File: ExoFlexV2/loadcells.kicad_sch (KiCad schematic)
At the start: 73 parts, among them U14 SN74LVC3G14DCUT_V2, U16 SN74LV4T08PWR_V2, U17 SN74HC7032D_V2, U24 MCP6001T-I_OT, U25 MCP6001T-I_OT, U26 MCP6001T-I_OT, U27 ADCMP602BRMZ, U28 ADCMP602BRMZ, U29 ADCMP602BRMZ

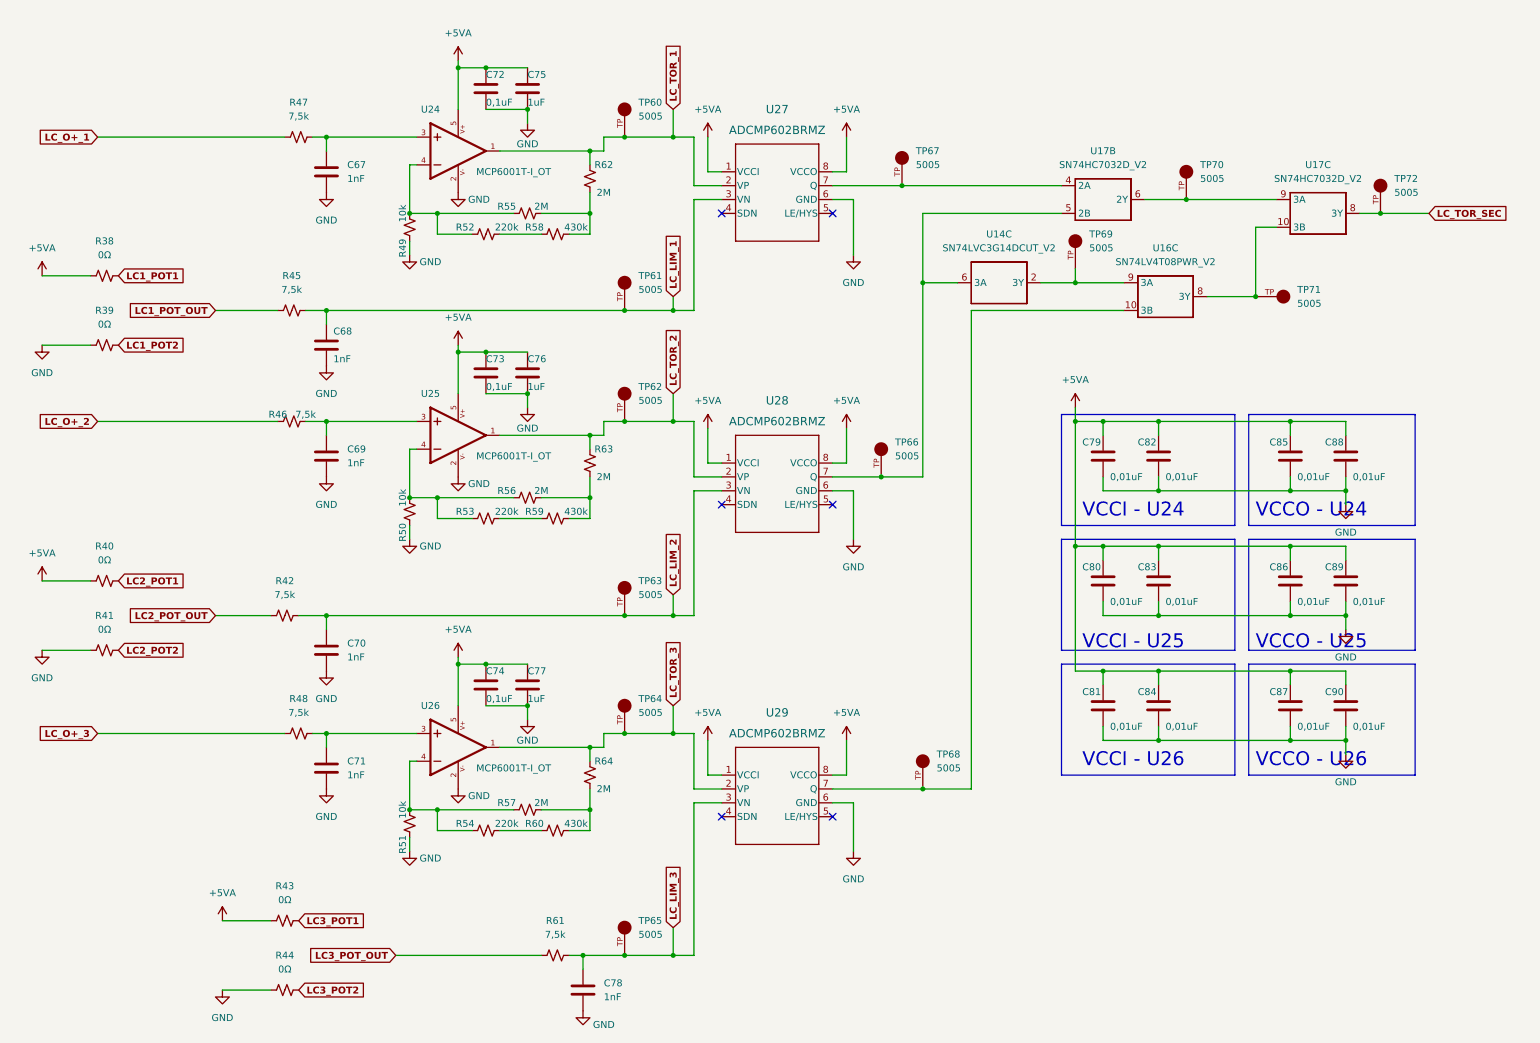
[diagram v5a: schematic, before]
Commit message: Mise à jour mi-stage
- Torque et Amplitude testé et vérifié
- Capteur de présence et de proximité testé
- Système de détection de coupure de fils
- Polyvalence pour plusieurs capteurs
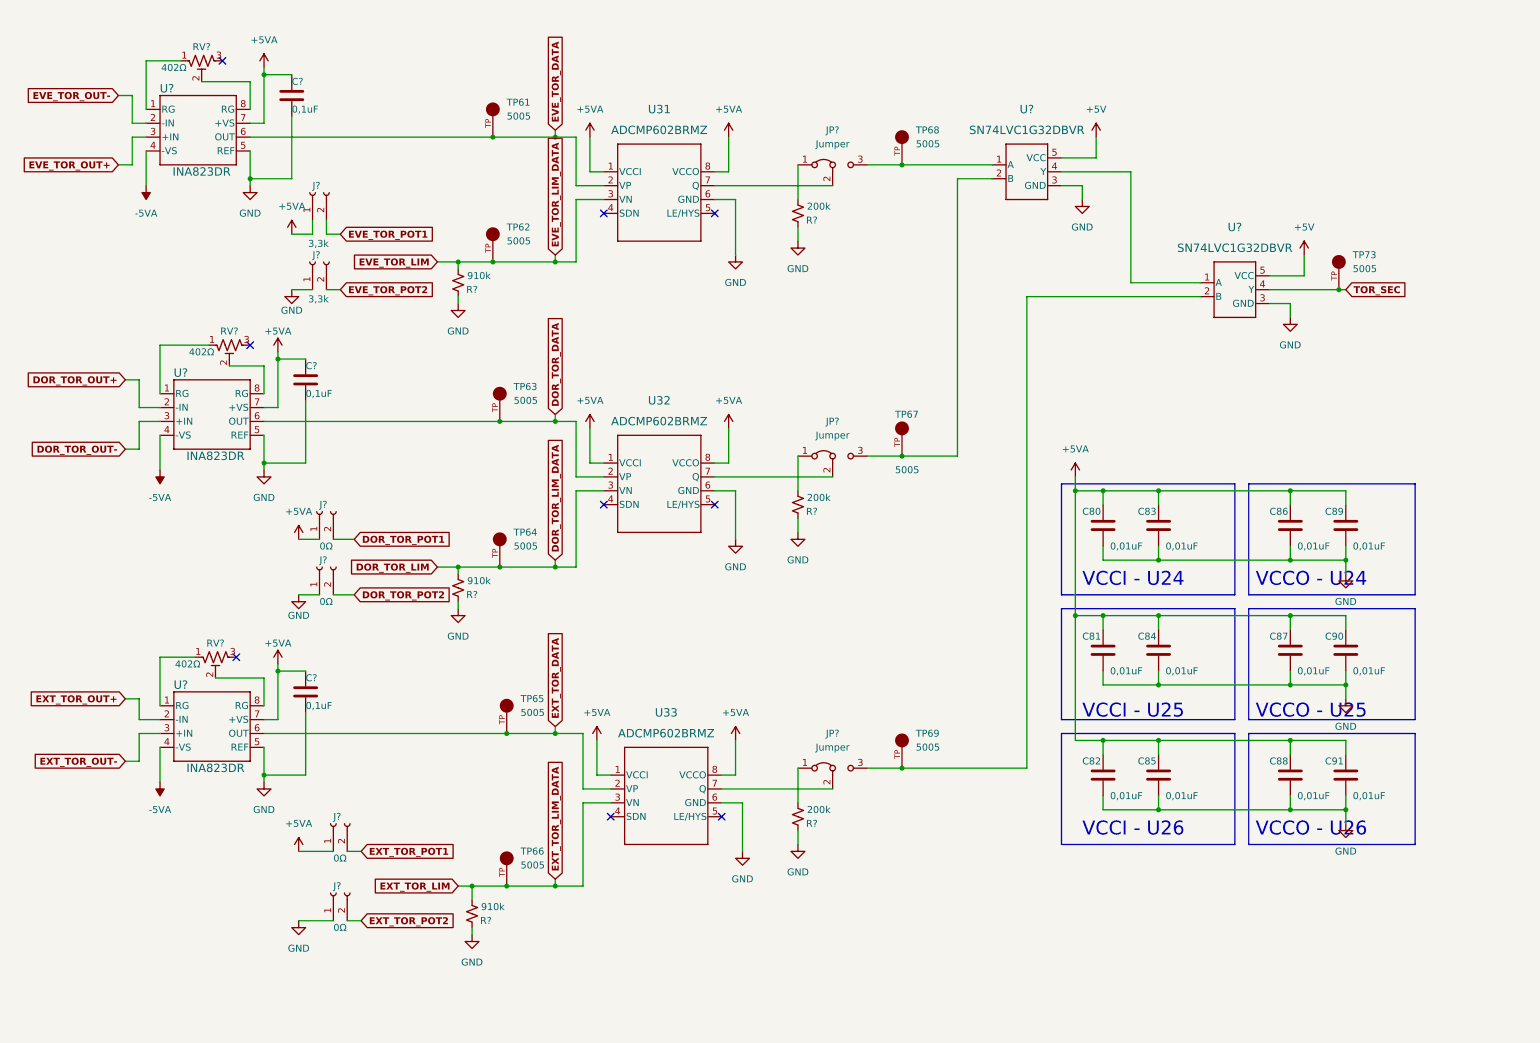
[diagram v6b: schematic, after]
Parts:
- removed C67, C68, C69, C70, C71, C78: 1nF, Capacitor_SMD:C_0603_1608Metric, symbol Device:C
- removed C72, C73, C74: 0,1uF, Capacitor_SMD:C_0603_1608Metric, symbol Device:C
- removed C75, C76, C77: 1uF, Capacitor_SMD:C_0603_1608Metric, symbol Device:C
- removed R38, R39, R40, R41, R43, R44: 0Ω, Resistor_SMD:R_0603_1608Metric, symbol Device:R_Small_US
- removed R42, R45, R46, R47, R48, R61: 7,5k, Resistor_SMD:R_0603_1608Metric, symbol Device:R_Small_US
- removed R49, R50, R51: 10k, Resistor_SMD:R_0603_1608Metric, symbol Device:R_Small_US
- removed R52, R53, R54: 220k, Resistor_SMD:R_0603_1608Metric, symbol Device:R_Small_US
- removed R55, R56, R57, R62, R63, R64: 2M, Resistor_SMD:R_0603_1608Metric, symbol Device:R_Small_US
- removed R58, R59, R60: 430k, Resistor_SMD:R_0603_1608Metric, symbol Device:R_Small_US
- removed TP69, TP70, TP71: 5005, FootPrint:KEYSTONE_5005, symbol SymLib:5005
- removed U14: SN74LVC3G14DCUT_V2, FootPrint:SN74LVC3G14DCUT, symbol SymLib:SN74LVC3G14DCUT_V2
- removed U16: SN74LV4T08PWR_V2, FootPrint:SN74LV4T08PWR, symbol SymLib:SN74LV4T08PWR_V2
- removed U17: SN74HC7032D_V2, FootPrint:SN74HC7032D, symbol SymLib:SN74HC7032D_V2
- removed U24, U25, U26: MCP6001T-I_OT, FootPrint:SOT95P270X145-5N, symbol SymLib:MCP6001T-I_OT
- added C? (x3): 0,1uF, Capacitor_SMD:C_0402_1005Metric, symbol Device:C
- added J? (x2): 3,3k, Connector_PinHeader_2.54mm:PinHeader_1x02_P2.54mm_Vertical, symbol Connector:Conn_01x02_Female
- added J? (x4): 0Ω, Connector_PinHeader_2.54mm:PinHeader_1x02_P2.54mm_Vertical, symbol Connector:Conn_01x02_Female
- added JP? (x3): Jumper, Connector_PinHeader_2.54mm:PinHeader_1x03_P2.54mm_Vertical, symbol Jumper:Jumper_3_Bridged12
- added R? (x3): 200k, Resistor_SMD:R_0603_1608Metric, symbol Device:R_Small_US
- added R? (x3): 910k, Resistor_SMD:R_0603_1608Metric, symbol Device:R_Small_US
- added RV? (x3): 402Ω, FootPrint:TRIM_3362P-1-102LF, symbol Device:R_Potentiometer_Trim_US
- added U? (x3): INA823DR, FootPrint:D0008A_SOIC_TEX, symbol SymLib:INA823DR
- added U? (x2): SN74LVC1G32DBVR, FootPrint:SOT95P270X145-5N, symbol SymLib:SN74LVC1G32DBVR
- renumbered C79 to C80, C80 to C81, C81 to C82, C82 to C83, C83 to C84, C84 to C85, C85 to C86, C86 to C87, C87 to C88, C88 to C89, C89 to C90, C90 to C91, TP60 to TP61, TP61 to TP62, TP62 to TP63, TP63 to TP64, TP64 to TP65, TP65 to TP66, TP66 to TP67, TP67 to TP68, TP68 to TP69, TP72 to TP73, U27 to U31, U28 to U32, U29 to U33
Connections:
- net +5VA: now also C?.1, C?.1, C?.1, J?.1 (Pin_1), J?.1 (Pin_1), J?.1 (Pin_1), U?.7 (+VS), U?.7 (+VS), U?.7 (+VS)
- net GND: now also C?.2, C?.2, C?.2, J?.1 (Pin_1), J?.1 (Pin_1), J?.1 (Pin_1), R?.2, R?.2, R?.2, R?.2, R?.2, R?.2, U?.3 (GND), U?.3 (GND), U?.5 (REF), U?.5 (REF), U?.5 (REF)
- net at TP67.TP: now also JP?.3 (B), U?.2 (B); no longer U32.7 (Q)
- net at U33.7 (Q): now also JP?.2 (C); no longer TP69.TP
- net at TP68.TP: now also JP?.3 (B), U?.1 (A); no longer U31.7 (Q)
- net LC_LIM_1 renamed EVE_TOR_LIM
- net EVE_TOR_LIM: now also R?.1
- net LC_LIM_2 renamed DOR_TOR_LIM
- net DOR_TOR_LIM: now also R?.1
- net LC_LIM_3 renamed EXT_TOR_LIM
- net EXT_TOR_LIM: now also R?.1
- net LC_TOR_1 renamed EVE_TOR_DATA
- net EVE_TOR_DATA: now also U?.6 (OUT)
- net LC_TOR_2 renamed DOR_TOR_DATA
- net DOR_TOR_DATA: now also U?.6 (OUT)
- net LC_TOR_3 renamed EXT_TOR_DATA
- net EXT_TOR_DATA: now also U?.6 (OUT)
- net LC_TOR_SEC renamed TOR_SEC
- net TOR_SEC: now also U?.4 (Y)
- new net: JP?.1 (A), R?.1 (x3)
- new net: RV?.1, U?.1 (RG) (x3)
- new net: RV?.2, U?.8 (RG) (x3)
- new net: JP?.3 (B), TP69.TP, U?.2 (B)
- new net: U?.1 (A), U?.4 (Y)
- new net: JP?.2 (C), U32.7 (Q)
- new net: JP?.2 (C), U31.7 (Q)
- new net +5V: U?.5 (VCC), U?.5 (VCC)
- new net -5VA: U?.4 (-VS), U?.4 (-VS), U?.4 (-VS)
- new net DOR_TOR_OUT+: U?.2 (-IN)
- new net DOR_TOR_OUT-: U?.3 (+IN)
- new net DOR_TOR_POT1: J?.2 (Pin_2)
- new net DOR_TOR_POT2: J?.2 (Pin_2)
- new net EVE_TOR_OUT+: U?.3 (+IN)
- new net EVE_TOR_OUT-: U?.2 (-IN)
- new net EVE_TOR_POT1: J?.2 (Pin_2)
- new net EVE_TOR_POT2: J?.2 (Pin_2)
- new net EXT_TOR_OUT+: U?.2 (-IN)
- new net EXT_TOR_OUT-: U?.3 (+IN)
- new net EXT_TOR_POT1: J?.2 (Pin_2)
- new net EXT_TOR_POT2: J?.2 (Pin_2)
- no-connect marks 6 -> 9
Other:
- moved on the sheet: C80, C81, C82, C83, C84, C85, C86, C87, C88, C89, C90, C91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

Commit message: Mise à jour signaux STM
- Condo de découplage
- Signaux supplémentaire pour le STM
- Page GND sera pour Multiplexeur
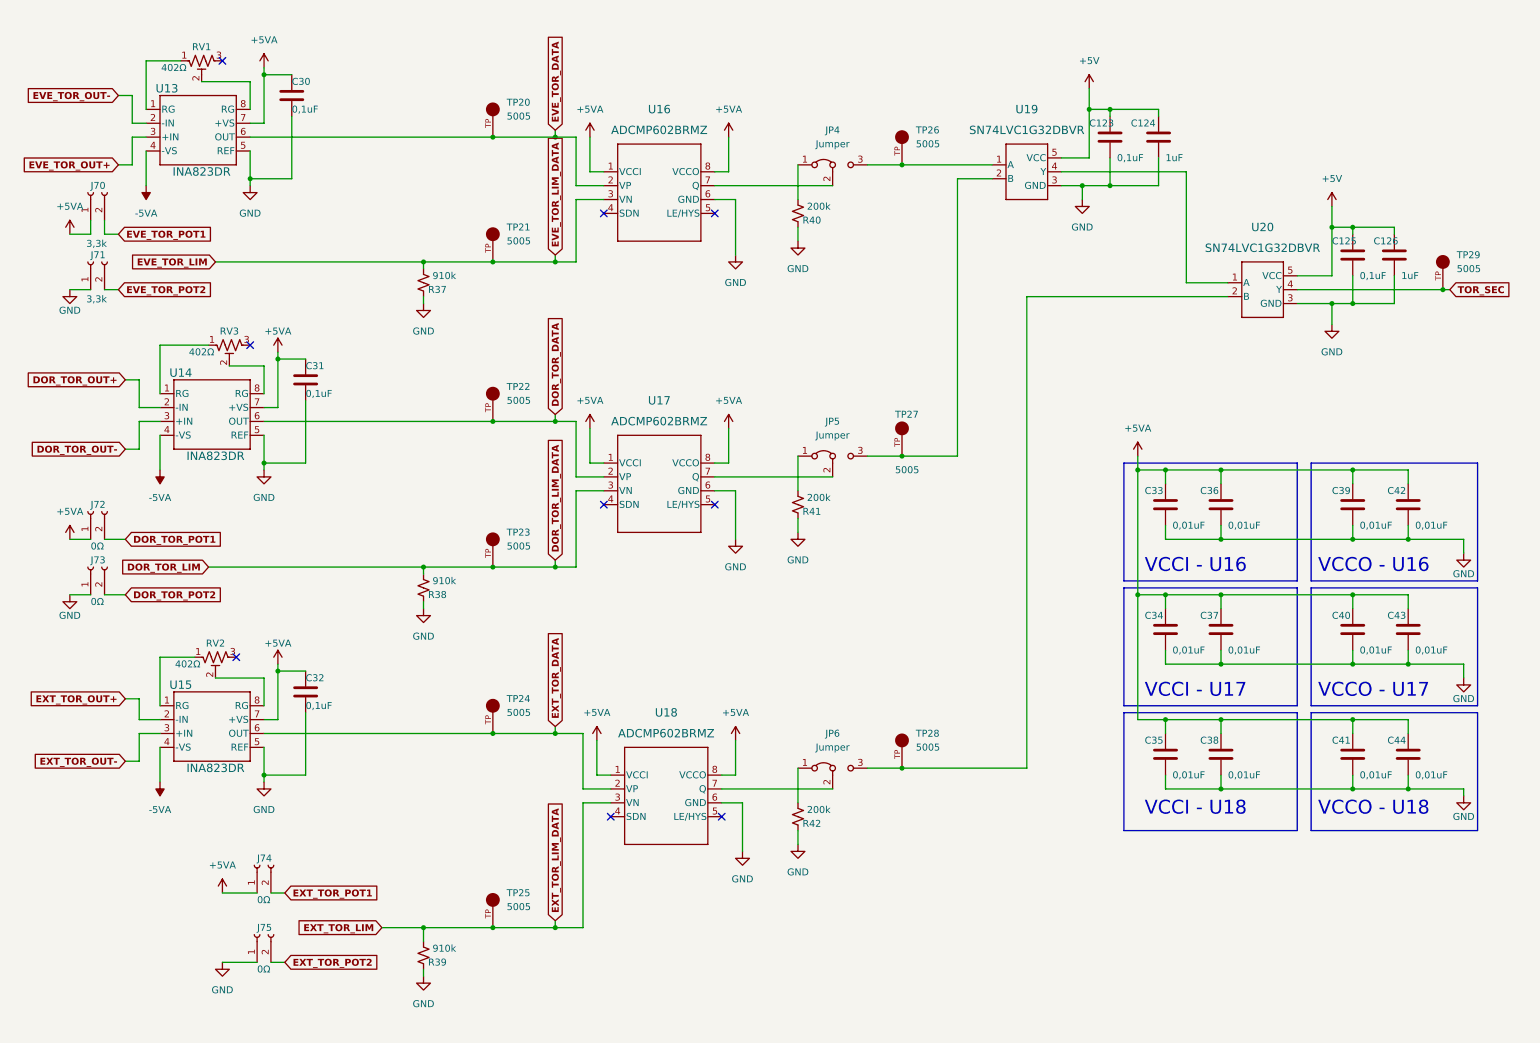
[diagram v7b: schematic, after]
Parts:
- added C123, C125: 0,1uF, Capacitor_SMD:C_0603_1608Metric, symbol Device:C
- added C124, C126: 1uF, Capacitor_SMD:C_0603_1608Metric, symbol Device:C
- gave numbers to parts that had none: 26
- renumbered C80 to C33, C81 to C34, C82 to C35, C83 to C36, C84 to C37, C85 to C38, C86 to C39, C87 to C40, C88 to C41, C89 to C42, C90 to C43, C91 to C44, TP61 to TP20, TP62 to TP21, TP63 to TP22, TP64 to TP23, TP65 to TP24, TP66 to TP25, TP68 to TP26, TP67 to TP27, TP69 to TP28, TP73 to TP29, U31 to U16, U32 to U17, U33 to U18
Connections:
- net +5V: now also C123.1, C124.1, C125.1, C126.1
- net GND: now also C123.2, C124.2, C125.2, C126.2
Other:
- note added: "VCCI - U16"
- note added: "VCCI - U17"
- note added: "VCCI - U18"
- note added: "VCCO - U16"
- note added: "VCCO - U17"
- note added: "VCCO - U18"
- note removed: "VCCI - U24"
- note removed: "VCCI - U25"
- note removed: "VCCI - U26"
- note removed: "VCCO - U24"
- note removed: "VCCO - U25"
- note removed: "VCCO - U26"
- moved on the sheet: C33, C34, C35, C36, C37, C38, C39, C40, C41, C42, C43, C44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

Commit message: Finalisation 1
- Ajout de pages pour la gestion des signaux négatif
- Modification des pages de torque et amplitude
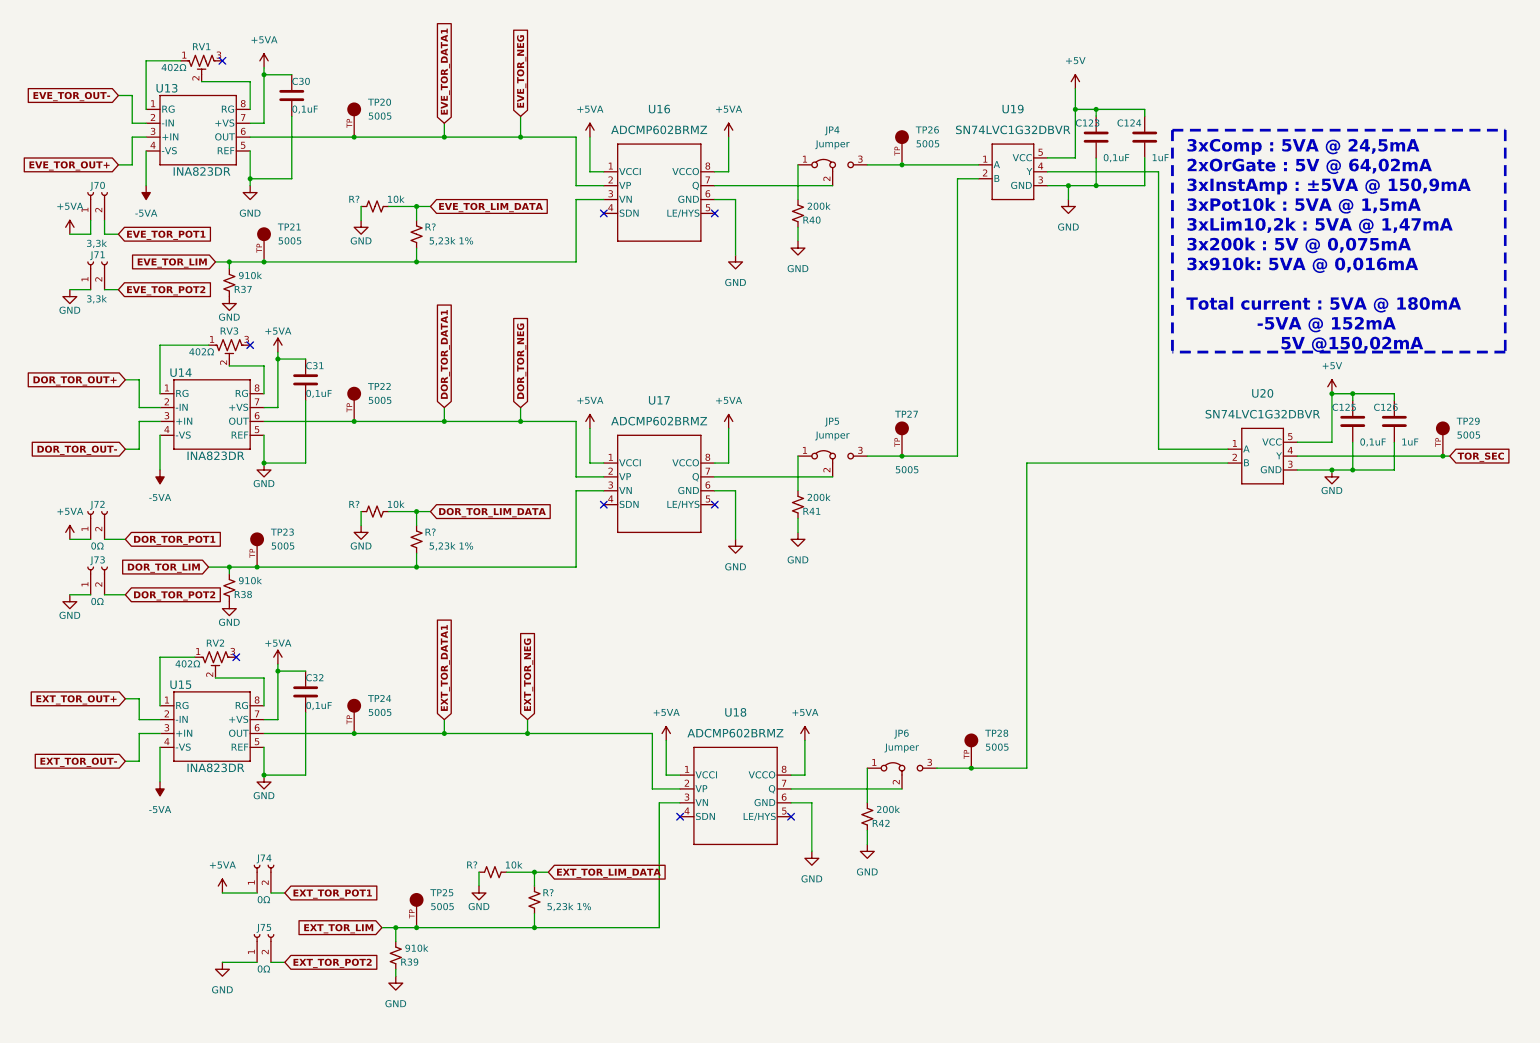
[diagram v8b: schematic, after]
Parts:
- removed C33, C34, C35, C36, C37, C38, C39, C40, C41, C42, C43, C44: 0,01uF, Capacitor_SMD:C_0603_1608Metric, symbol Device:C
- added R? (x3): 5,23k 1%, Resistor_SMD:R_0805_2012Metric, symbol Device:R_Small_US
- added R? (x3): 10k, Resistor_SMD:R_0805_2012Metric, symbol Device:R_Small_US
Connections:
- net DOR_TOR_LIM: now also R?.2
- net EVE_TOR_LIM: now also R?.2
- net EXT_TOR_LIM: now also R?.2
- net GND: now also R?.1, R?.1, R?.1
- net DOR_TOR_DATA renamed DOR_TOR_DATA1
- net EVE_TOR_DATA renamed EVE_TOR_DATA1
- net EXT_TOR_DATA renamed EXT_TOR_DATA1
- new net DOR_TOR_LIM_DATA: R?.1, R?.2
- new net EVE_TOR_LIM_DATA: R?.1, R?.2
- new net EXT_TOR_LIM_DATA: R?.1, R?.2
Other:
- note added: "3xComp : 5VA @ 24,5mA 2xOrGate : 5V @ 64,02mA 3xInstAmp : ±5VA @ 150,9mA 3xPot10k : 5VA @ 1,5mA 3xLim10,2k : 5VA @ 1,47mA 3x200k : 5V @ 0,075mA 3x910k: 5VA @ 0,016mA Total current : 5VA @ 180mA -5VA @ 152mA 5V @150,02mA"
- note removed: "VCCI - U16"
- note removed: "VCCI - U17"
- note removed: "VCCI - U18"
- note removed: "VCCO - U16"
- note removed: "VCCO - U17"
- note removed: "VCCO - U18"
- moved on the sheet: C123, C124, C125, C126, JP6, R37, R38, R39, R42, TP20, TP21, TP22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
